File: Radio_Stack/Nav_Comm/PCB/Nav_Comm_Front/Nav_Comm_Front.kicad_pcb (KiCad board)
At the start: 2 copper layers, 72.4 x 44.5 mm, 11 parts, among them SW1 Switch, SW2 Encoder

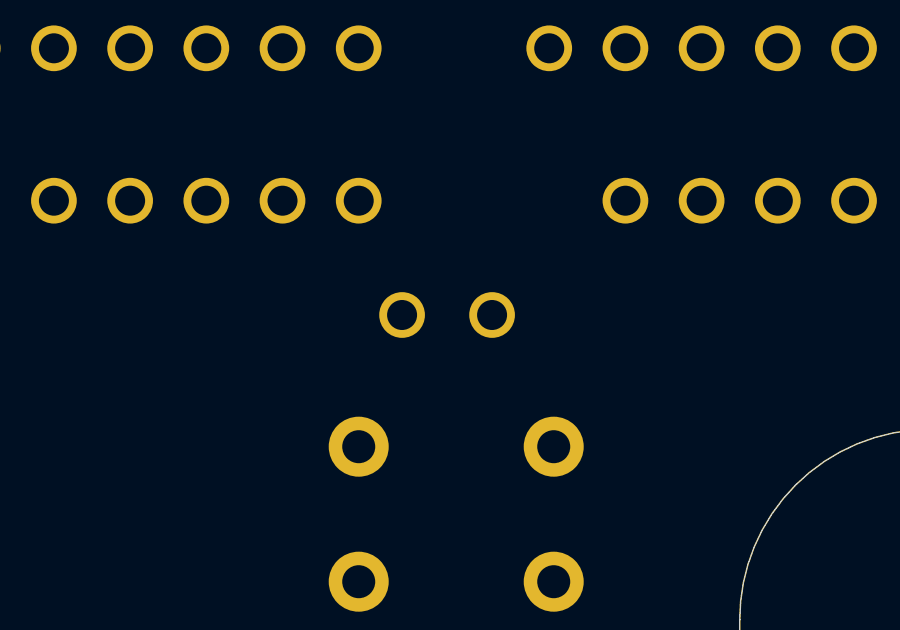
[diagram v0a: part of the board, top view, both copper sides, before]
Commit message: custom electronic components 3D models
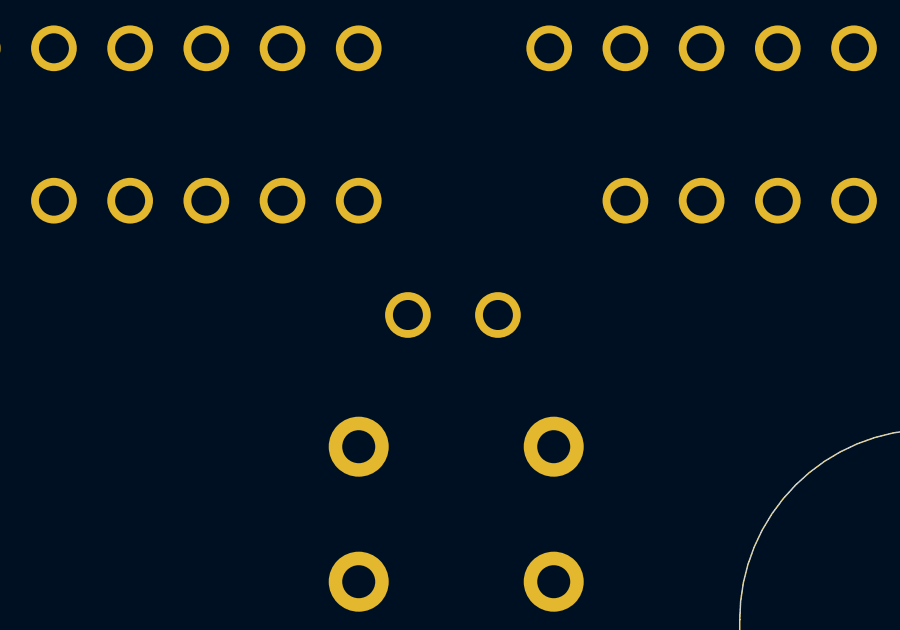
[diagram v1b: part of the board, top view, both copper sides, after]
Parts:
- moved R10 0.19 mm to (153.0, 81.3)

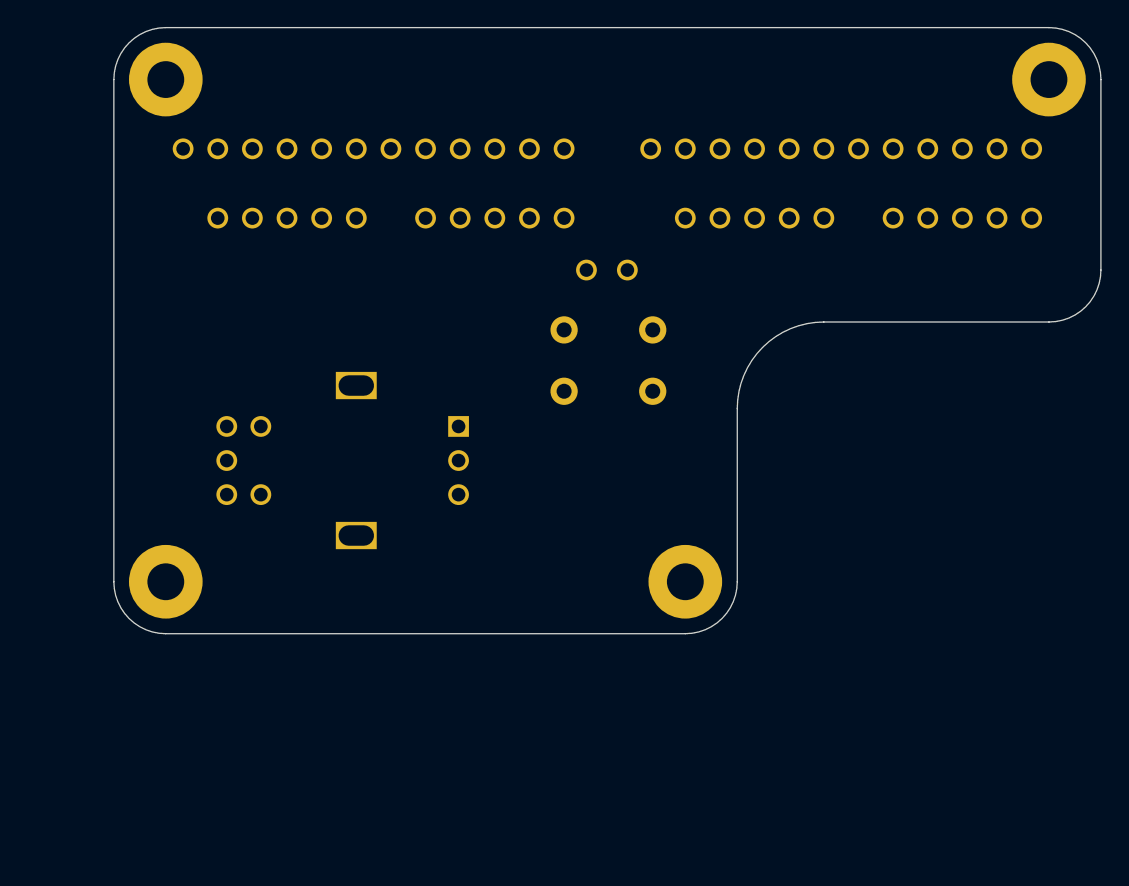
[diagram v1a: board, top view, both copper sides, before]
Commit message: custom electronic components 3D models, Nav-Comm module PCB's
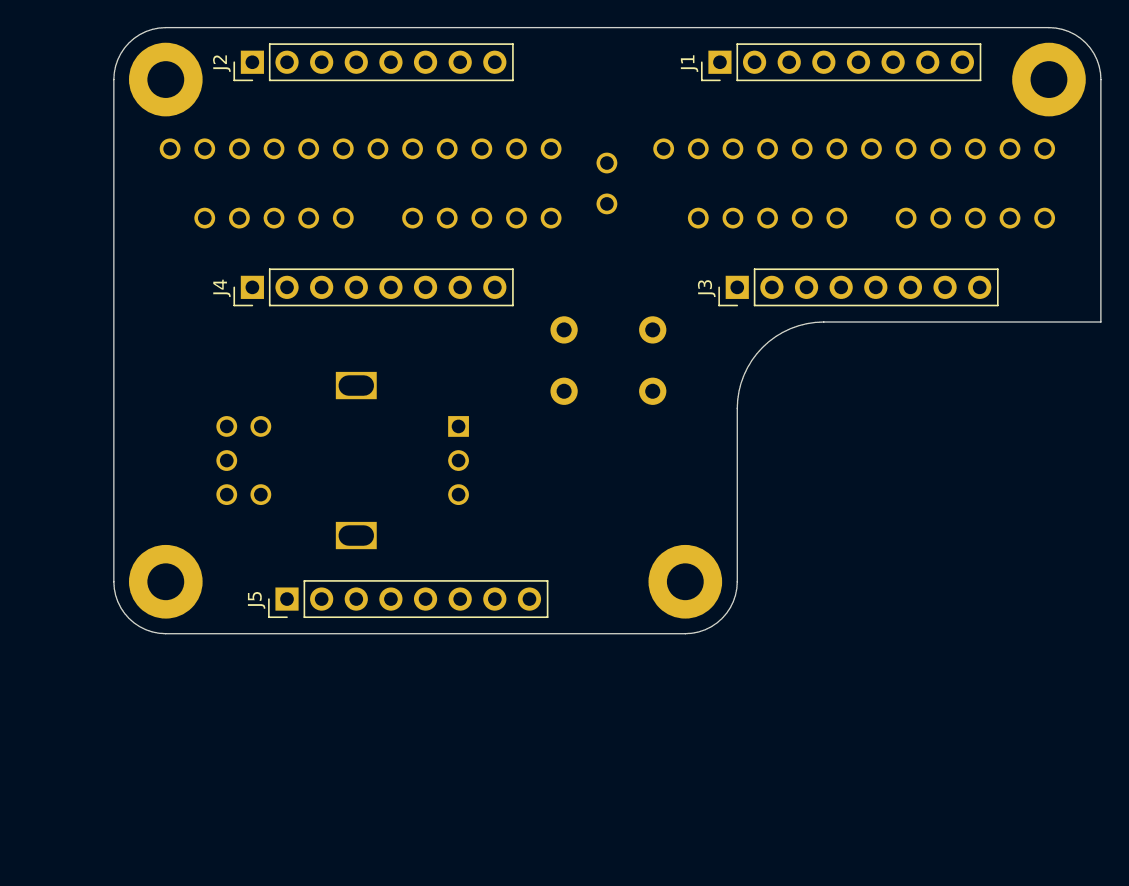
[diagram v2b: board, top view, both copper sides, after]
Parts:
- added J1: Conn_01x08, Connector_PinHeader_2.54mm:PinHeader_1x08_P2.54mm_Vertical, F.Cu at (161.3, 66.0)
- added J2: Conn_01x08, Connector_PinHeader_2.54mm:PinHeader_1x08_P2.54mm_Vertical, F.Cu at (127.0, 66.0)
- added J3: Conn_01x08, Connector_PinHeader_2.54mm:PinHeader_1x08_P2.54mm_Vertical, F.Cu at (162.6, 82.5)
- added J4: Conn_01x08, Connector_PinHeader_2.54mm:PinHeader_1x08_P2.54mm_Vertical, F.Cu at (127.0, 82.5)
- added J5: Conn_01x08, Connector_PinHeader_2.54mm:PinHeader_1x08_P2.54mm_Vertical, F.Cu at (129.5, 105.4)
- R10: value R_PHOTO -> R_LIT
- SW1: value Switch -> FREQ
- moved R10 6.35 mm to (153.0, 74.9), turned to 90 degrees
- moved D22 0.95 mm to (127.3, 74.9)
- moved D11 0.95 mm to (178.8, 74.9)
- moved D12 0.95 mm to (163.5, 74.9)
- moved D21 0.95 mm to (142.6, 74.9)
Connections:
- net Net-(SW1-Pad1) renamed /FREQ_SW
- R10 pad 1: (no net) -> VCC
- SW1 pad 2: Net-(SW1-Pad2) -> GND
- SW2 pad 3: (no net) -> GND
- SW2 pad 4: (no net) -> GND
- SW2 pad 8: (no net) -> GND
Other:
- outline, holes or cut-outs redrawn

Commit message: Nav-Comm module PCB's
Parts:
- moved J3 16.1 mm to (157.5, 97.8)
- moved J4 16.1 mm to (121.9, 97.8)
- moved J5 16.1 mm to (124.5, 120.7)
- moved D21 16.1 mm to (137.5, 90.2)
- moved H1 16.1 mm to (115.6, 82.5)
- moved H3 16.1 mm to (115.6, 119.4)
- moved H4 16.1 mm to (153.7, 119.4)
- moved R10 16.1 mm to (147.9, 90.2)
- moved SW1 16.1 mm to (144.8, 105.4)
- moved SW2 16.1 mm to (129.5, 110.5)
- moved D22 16.1 mm to (122.2, 90.2)
- moved J2 16.1 mm to (121.9, 81.3)
- moved D11 16.1 mm to (173.7, 90.2)
- moved D12 16.1 mm to (158.4, 90.2)
- moved H2 16.1 mm to (180.3, 82.5)
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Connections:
- D11 pad 12: (no net) -> /D1_DIG_0
- D11 pad 8: (no net) -> /D1_DIG_2
- D11 pad 9: (no net) -> /D1_DIG_1
- D12 pad 12: (no net) -> /D1_DIG_3
- D12 pad 8: (no net) -> /D1_DIG_5
- D12 pad 9: (no net) -> /D1_DIG_4
- D21 pad 12: (no net) -> /D2_DIG_0
- D21 pad 8: (no net) -> /D2_DIG_2
- D21 pad 9: (no net) -> /D2_DIG_1
- D22 pad 12: (no net) -> /D2_DIG_3
- D22 pad 8: (no net) -> /D2_DIG_5
- D22 pad 9: (no net) -> /D2_DIG_4
- J1 pad 1: /D1_SEG_A -> /D1_SEG_B
- J1 pad 2: /D1_SEG_B -> /D1_DIG_5
- J1 pad 3: /D1_SEG_C -> /D1_DIG_4
- J1 pad 4: /D1_SEG_D -> /D1_SEG_F
- J1 pad 5: /D1_SEG_E -> /D1_SEG_A
- J1 pad 6: /D1_SEG_F -> /D1_DIG_3
- J1 pad 7: /D1_SEG_G -> /D1_DIG_2
- J1 pad 8: /D1_DP -> /D1_DIG_1
- J2 pad 1: (no net) -> /D2_SEG_B
- J2 pad 2: (no net) -> /D2_DIG_5
- J2 pad 3: (no net) -> /D2_DIG_4
- J2 pad 4: (no net) -> /D2_SEG_F
- J2 pad 5: (no net) -> /D2_SEG_A
- J2 pad 6: (no net) -> /D2_DIG_3
- J2 pad 7: (no net) -> /D2_DIG_2
- J2 pad 8: (no net) -> /D2_DIG_1
- J3 pad 2: (no net) -> /D1_SEG_C
- J3 pad 3: (no net) -> /D1_SEG_D
- J3 pad 4: (no net) -> /D1_SEG_G
- J3 pad 5: (no net) -> /D1_DP
- J3 pad 6: (no net) -> /D1_SEG_E
- J3 pad 7: (no net) -> /D1_DIG_0
- J4 pad 2: (no net) -> /D2_SEG_C
- J4 pad 3: (no net) -> /D2_SEG_D
- J4 pad 4: (no net) -> /D2_SEG_G
- J4 pad 5: (no net) -> /D2_DP
- J4 pad 6: (no net) -> /D2_SEG_E
- J4 pad 7: (no net) -> /D2_DIG_0
- J5 pad 1: (no net) -> /FREQ_A1
- J5 pad 2: (no net) -> /FREQ_B1
- J5 pad 3: (no net) -> /FREQ_E
- J5 pad 4: (no net) -> /FREQ_A
- J5 pad 5: (no net) -> /FREQ_B
- J5 pad 6: (no net) -> /FREQ_SW
- J5 pad 7: (no net) -> /RV_LIT
- J5 pad 8: (no net) -> GND
- R10 pad 2: (no net) -> /RV_LIT
- SW2 pad 1: (no net) -> /FREQ_A
- SW2 pad 2: (no net) -> /FREQ_B
- SW2 pad 5: (no net) -> /FREQ_E
- SW2 pad 6: (no net) -> /FREQ_A1
- SW2 pad 7: (no net) -> /FREQ_B1
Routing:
- net VCC: track 0.00 -> 43.8 mm
- net /RV_LIT: track 0.00 -> 37.0 mm
- net /D1_DP: track 0.00 -> 26.8 mm
- net /D2_DP: track 0.00 -> 26.1 mm
- net /FREQ_SW: track 0.00 -> 25.9 mm
- net /D2_SEG_B: track 0.00 -> 25.8 mm
- net /D1_SEG_B: track 0.00 -> 24.9 mm
- net /D2_SEG_D: track 0.00 -> 24.2 mm
- net /D1_SEG_D: track 0.00 -> 24.0 mm
- net /D2_SEG_C: track 0.00 -> 23.9 mm
- net /D1_SEG_C: track 0.00 -> 23.6 mm
- net /D1_SEG_A: track 0.00 -> 23.5 mm
- net /D1_SEG_F: track 0.00 -> 23.1 mm
- net /D2_SEG_A: track 0.00 -> 22.5 mm
- net /D2_SEG_F: track 0.00 -> 22.4 mm
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- added copper zone on B.Cu, net GND
- added copper zone on F.Cu, net GND
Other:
- outline, holes or cut-outs redrawn
- net class Default: trace_width 0.25 -> 0.5
- board text added: "NavComm Front rev. 1"
- board text added: "marekcel.pl"

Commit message: custom electronic components KiCAD symbols, custom electronic components KiCAD footprints, Nav-Comm module PCB's
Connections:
- SW2 pad MP: (no net) -> GND
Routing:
- net /RV_LIT: track 37.0 -> 35.4 mm
- net /D1_SEG_A: track 23.5 -> 22.5 mm
- net /D1_DIG_0: track 19.9 -> 19.1 mm
- net /D1_SEG_F: track 23.1 -> 22.5 mm
